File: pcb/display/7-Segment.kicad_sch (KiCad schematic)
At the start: 28 parts, among them J401 XH 2P, J402 XH 2P, J403 XH 2P, J404 XH 2P, J405 XH 2P, J406 XH 2P, J407 XH 2P, Q401 DOZ35N06, Q402 DOZ35N06, Q403 DOZ35N06, Q404 DOZ35N06, Q405 DOZ35N06, Q406 DOZ35N06, Q407 DOZ35N06

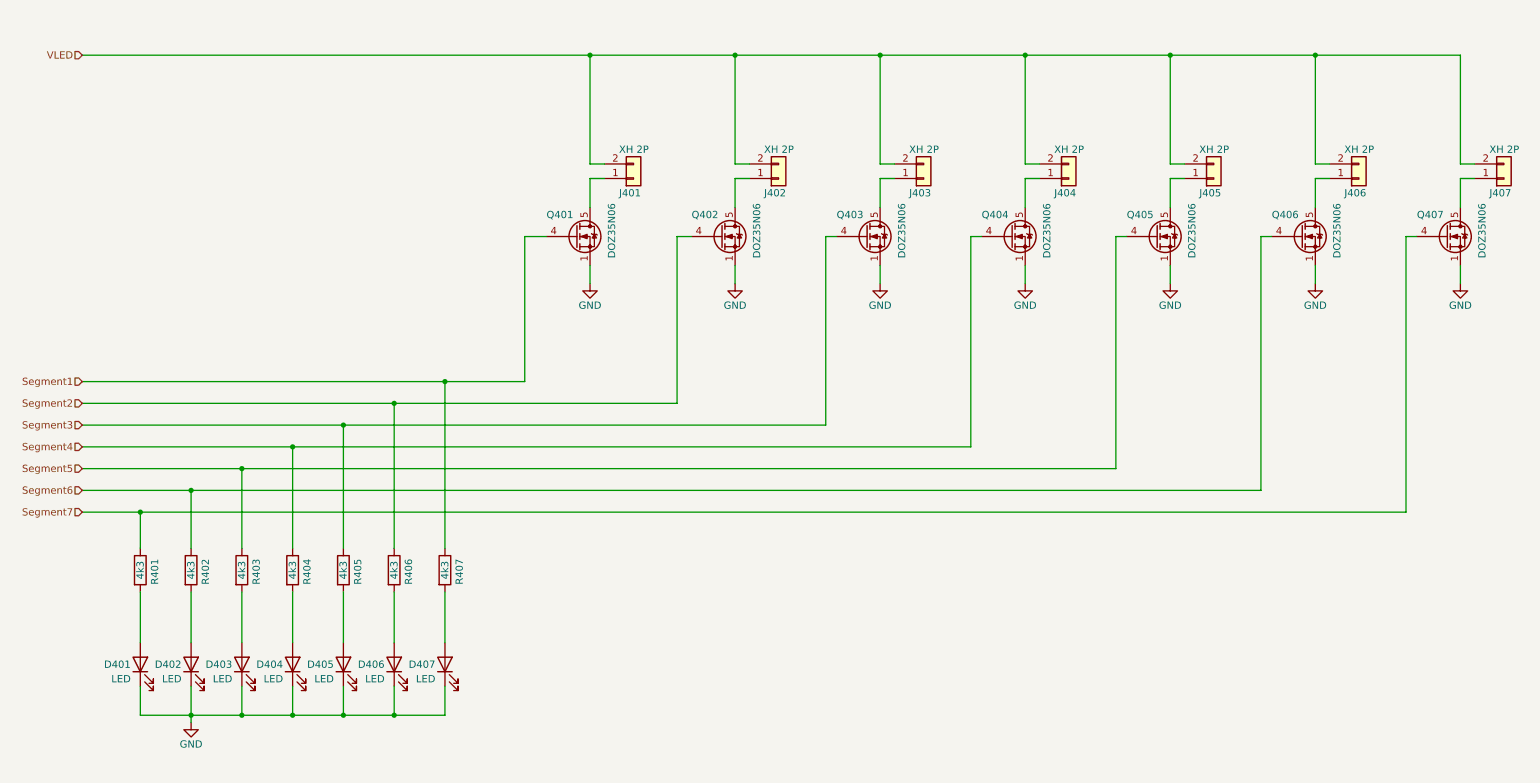
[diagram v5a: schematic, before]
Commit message: OSC Display Hardware Revision 02
There might still be some errors which need to be corrected during ordering.
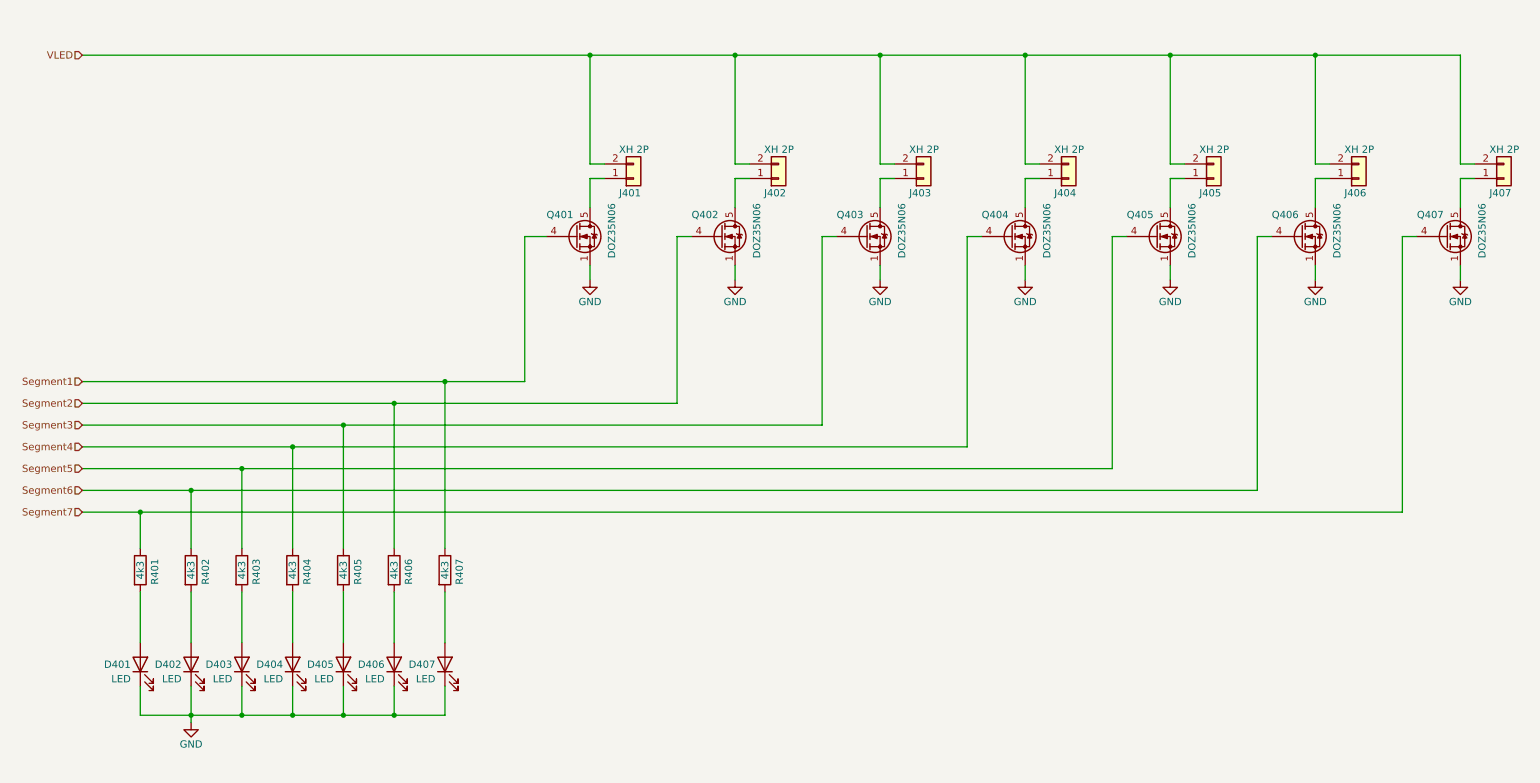
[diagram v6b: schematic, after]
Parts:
- D401, D402, D403, D404, D405, D406, D407: JLC PN C2286 -> (none); LCSC Part # (none) -> C2286
- J401, J402, J403, J404, J405, J406, J407: JLC PN C158012 -> (none); LCSC Part # (none) -> C158012
- Q401, Q402, Q403, Q404, Q405, Q406, Q407: JLC PN C36499167 -> (none); LCSC Part # (none) -> C36499167

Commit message: Adjusted footprint of mosfets for 0.15mm solder mask spacing
New Gerber files
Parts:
- Q401, Q402, Q403, Q404, Q405, Q406, Q407: footprint Package_SON:VSON-8_3.3x3.3mm_P0.65mm_NexFET -> RVNSPRK_Packages:VSON-8_3.3x3.3mm_P0.65mm_Custom
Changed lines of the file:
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@@
 			)
 		)
-		(property "Footprint" "Package_SON:VSON-8_3.3x3.3mm_P0.65mm_NexFET"
+		(property "Footprint" "RVNSPRK_Packages:VSON-8_3.3x3.3mm_P0.65mm_Custom"
 			(at 142.24 54.61 0)
 			(effects
@@
 			)
 		)
-		(property "Footprint" "Package_SON:VSON-8_3.3x3.3mm_P0.65mm_NexFET"
+		(property "Footprint" "RVNSPRK_Packages:VSON-8_3.3x3.3mm_P0.65mm_Custom"
 			(at 167.64 54.61 0)
 			(effects
@@
 			)
 		)
-		(property "Footprint" "Package_SON:VSON-8_3.3x3.3mm_P0.65mm_NexFET"
+		(property "Footprint" "RVNSPRK_Packages:VSON-8_3.3x3.3mm_P0.65mm_Custom"
 			(at 243.84 54.61 0)
 			(effects
@@
 			)
 		)
-		(property "Footprint" "Package_SON:VSON-8_3.3x3.3mm_P0.65mm_NexFET"
+		(property "Footprint" "RVNSPRK_Packages:VSON-8_3.3x3.3mm_P0.65mm_Custom"
 			(at 218.44 54.61 0)
 			(effects
@@
 			)
 		)
-		(property "Footprint" "Package_SON:VSON-8_3.3x3.3mm_P0.65mm_NexFET"
+		(property "Footprint" "RVNSPRK_Packages:VSON-8_3.3x3.3mm_P0.65mm_Custom"
 			(at 269.24 54.61 0)
 			(effects
@@
 			)
 		)
-		(property "Footprint" "Package_SON:VSON-8_3.3x3.3mm_P0.65mm_NexFET"
+		(property "Footprint" "RVNSPRK_Packages:VSON-8_3.3x3.3mm_P0.65mm_Custom"
 			(at 193.04 54.61 0)
 			(effects
@@
 			)
 		)
-		(property "Footprint" "Package_SON:VSON-8_3.3x3.3mm_P0.65mm_NexFET"
+		(property "Footprint" "RVNSPRK_Packages:VSON-8_3.3x3.3mm_P0.65mm_Custom"
 			(at 116.84 54.61 0)
 			(effects
